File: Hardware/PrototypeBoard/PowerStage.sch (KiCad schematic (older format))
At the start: 20 parts, among them Q1 IRF8721PBF-1, Q2 IRF8721PBF-1, Q3 IRF8721PBF-1, Q4 IRF8721PBF-1, Q5 IRF8721PBF-1, Q6 IRF8721PBF-1

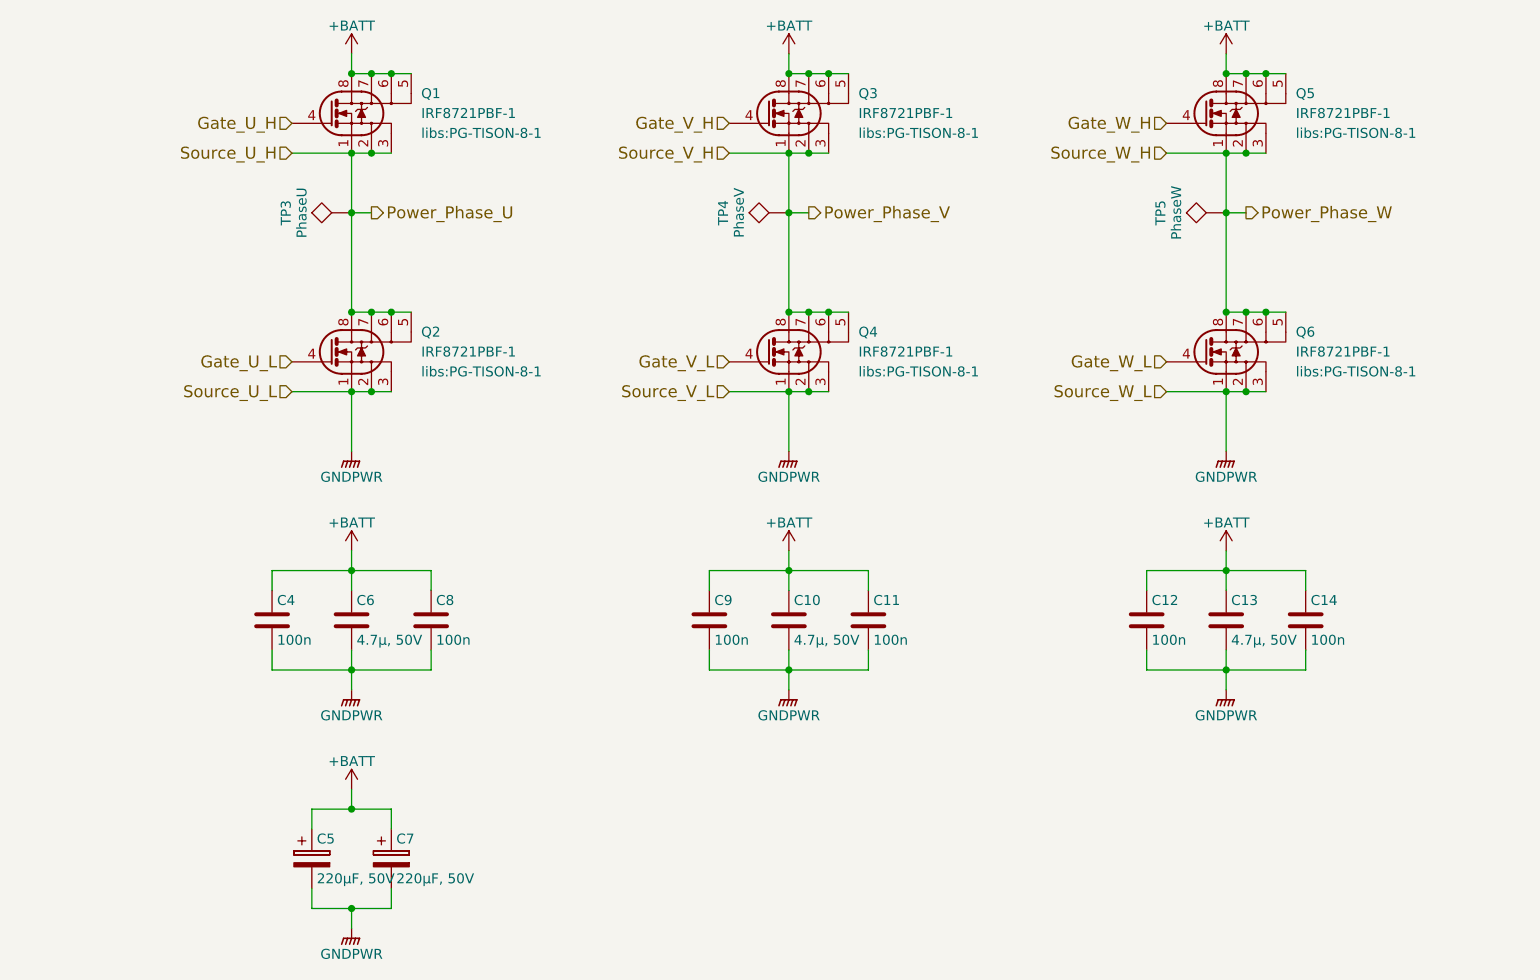
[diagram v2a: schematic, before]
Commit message: Added footprint for power MOSFETs
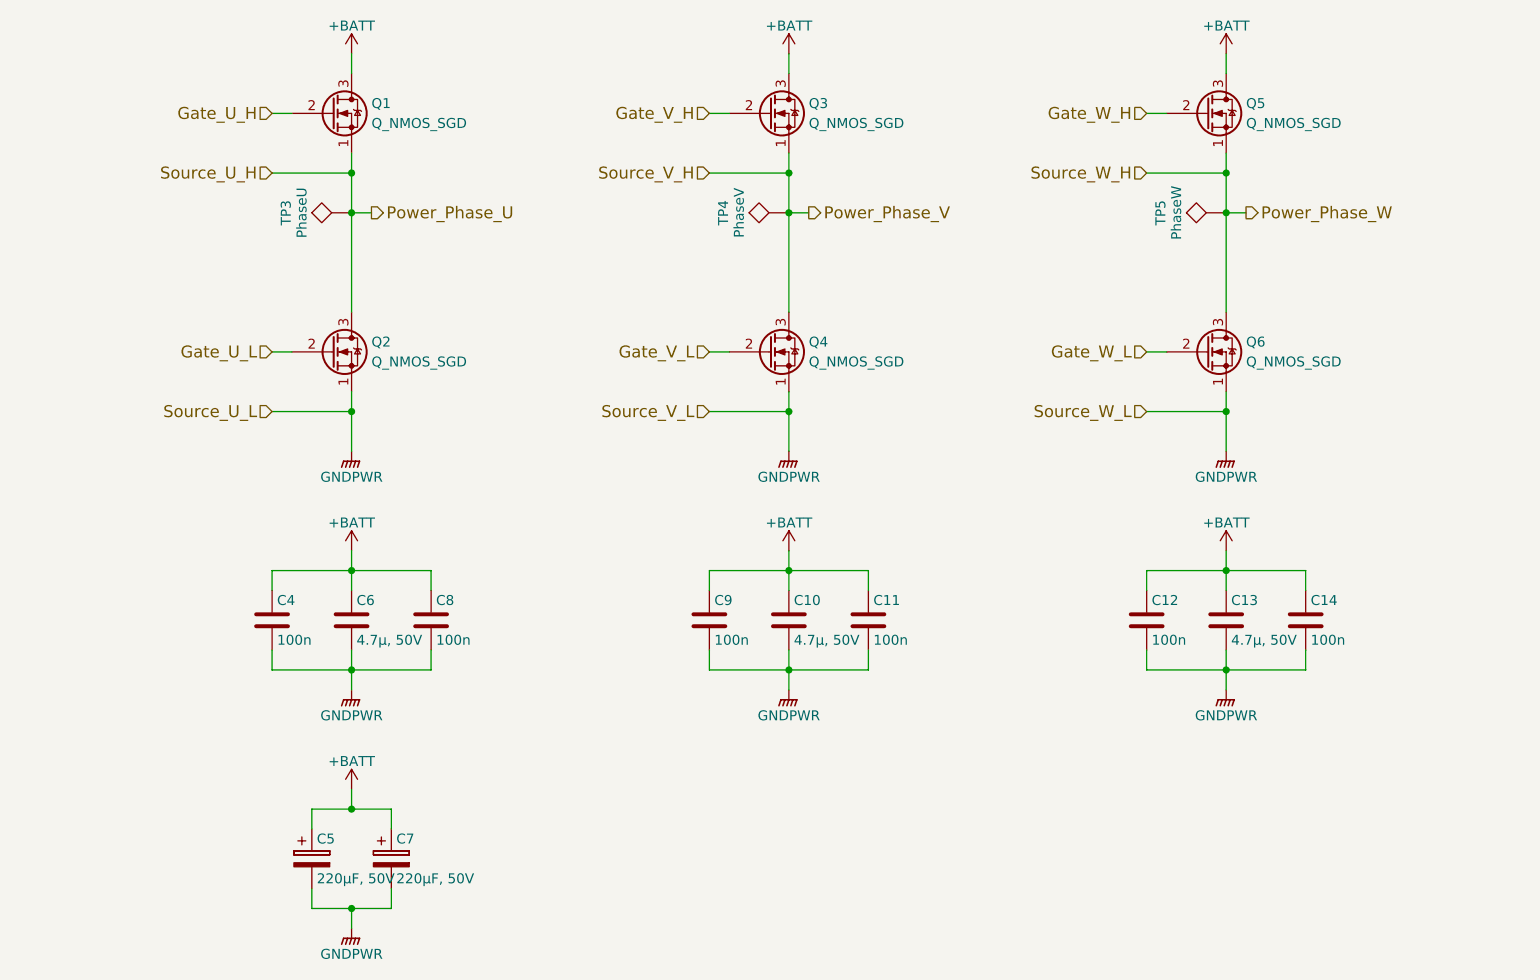
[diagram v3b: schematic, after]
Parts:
- removed Q1, Q2, Q3, Q4, Q5, Q6: IRF8721PBF-1, libs:PG-TISON-8-1, symbol IRF8721PBF-1
- added Q1, Q2, Q3, Q4, Q5, Q6: Q_NMOS_SGD, symbol Q_NMOS_SGD
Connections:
- net +BATT: now also Q1.3 (D), Q3.3 (D), Q5.3 (D)
- net GNDPWR: now also Q2.1 (S), Q4.1 (S), Q6.1 (S)
- net Gate_U_H: now also Q1.2 (G)
- net Gate_U_L: now also Q2.2 (G)
- net Gate_V_H: now also Q3.2 (G)
- net Gate_V_L: now also Q4.2 (G)
- net Gate_W_H: now also Q5.2 (G)
- net Gate_W_L: now also Q6.2 (G)
- net Power_Phase_U: now also Q1.1 (S), Q2.3 (D)
- net Power_Phase_V: now also Q3.1 (S), Q4.3 (D)
- net Power_Phase_W: now also Q5.1 (S), Q6.3 (D)
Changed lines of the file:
@@
 $EndDescr
 $Comp
-L IRF8721PBF-1 Q5
-U 1 1 56C10AD6
-P 7500 2400
-F 0 "Q5" H 7850 2500 50  0000 L CNN
-F 1 "IRF8721PBF-1" H 7850 2400 50  0000 L CNN
-F 2 "libs:PG-TISON-8-1" H 7850 2300 50  0000 L CNN
-F 3 "" H 7400 2400 50  0000 L CNN
-	1    7500 2400
-	1    0    0    -1
-$EndComp
-$Comp
-L IRF8721PBF-1 Q6
-U 1 1 56C10ADD
-P 7500 3600
-F 0 "Q6" H 7850 3700 50  0000 L CNN
-F 1 "IRF8721PBF-1" H 7850 3600 50  0000 L CNN
-F 2 "libs:PG-TISON-8-1" H 7850 3500 50  0000 L CNN
-F 3 "" H 7400 3600 50  0000 L CNN
-	1    7500 3600
-	1    0    0    -1
-$EndComp
-$Comp
-L IRF8721PBF-1 Q4
-U 1 1 56C10AE4
-P 5300 3600
-F 0 "Q4" H 5650 3700 50  0000 L CNN
-F 1 "IRF8721PBF-1" H 5650 3600 50  0000 L CNN
-F 2 "libs:PG-TISON-8-1" H 5650 3500 50  0000 L CNN
-F 3 "" H 5200 3600 50  0000 L CNN
-	1    5300 3600
-	1    0    0    -1
-$EndComp
-$Comp
-L IRF8721PBF-1 Q3
-U 1 1 56C10AEB
-P 5300 2400
-F 0 "Q3" H 5650 2500 50  0000 L CNN
-F 1 "IRF8721PBF-1" H 5650 2400 50  0000 L CNN
-F 2 "libs:PG-TISON-8-1" H 5650 2300 50  0000 L CNN
-F 3 "" H 5200 2400 50  0000 L CNN
-	1    5300 2400
-	1    0    0    -1
-$EndComp
-$Comp
-L IRF8721PBF-1 Q1
-U 1 1 56C10AF2
-P 3100 2400
-F 0 "Q1" H 3450 2500 50  0000 L CNN
-F 1 "IRF8721PBF-1" H 3450 2400 50  0000 L CNN
-F 2 "libs:PG-TISON-8-1" H 3450 2300 50  0000 L CNN
-F 3 "" H 3000 2400 50  0000 L CNN
-	1    3100 2400
-	1    0    0    -1
-$EndComp
-$Comp
-L IRF8721PBF-1 Q2
-U 1 1 56C10AF9
-P 3100 3600
-F 0 "Q2" H 3450 3700 50  0000 L CNN
-F 1 "IRF8721PBF-1" H 3450 3600 50  0000 L CNN
-F 2 "libs:PG-TISON-8-1" H 3450 3500 50  0000 L CNN
-F 3 "" H 3000 3600 50  0000 L CNN
-	1    3100 3600
-	1    0    0    -1
-$EndComp
-$Comp
-L GNDPWR #PWR012
+L GNDPWR #PWR13
 U 1 1 56C10B12
 P 3100 4100
-F 0 "#PWR012" H 3100 3900 50  0001 C CNN
+F 0 "#PWR13" H 3100 3900 50  0001 C CNN
 F 1 "GNDPWR" H 3100 3970 50  0000 C CNN
 F 2 "" H 3100 4050 50  0000 C CNN
@@
 $EndComp
 $Comp
-L GNDPWR #PWR013
+L GNDPWR #PWR19
 U 1 1 56C10B18
 P 5300 4100
-F 0 "#PWR013" H 5300 3900 50  0001 C CNN
+F 0 "#PWR19" H 5300 3900 50  0001 C CNN
 F 1 "GNDPWR" H 5300 3970 50  0000 C CNN
 F 2 "" H 5300 4050 50  0000 C CNN
@@
 $EndComp
 $Comp
-L GNDPWR #PWR014
+L GNDPWR #PWR23
 U 1 1 56C10B1E
 P 7500 4100
-F 0 "#PWR014" H 7500 3900 50  0001 C CNN
+F 0 "#PWR23" H 7500 3900 50  0001 C CNN
 F 1 "GNDPWR" H 7500 3970 50  0000 C CNN
 F 2 "" H 7500 4050 50  0000 C CNN
@@
 Text HLabel 5400 2900 2    60   Output ~ 0
 Power_Phase_V
-Text HLabel 2800 2450 0    60   Input ~ 0
+Text HLabel 2700 2400 0    60   Input ~ 0
 Gate_U_H
-Text HLabel 2800 3650 0    60   Input ~ 0
+Text HLabel 2700 3600 0    60   Input ~ 0
 Gate_U_L
-Text HLabel 5000 2450 0    60   Input ~ 0
+Text HLabel 4900 2400 0    60   Input ~ 0
 Gate_V_H
-Text HLabel 5000 3650 0    60   Input ~ 0
+Text HLabel 4900 3600 0    60   Input ~ 0
 Gate_V_L
-Text HLabel 7200 2450 0    60   Input ~ 0
+Text HLabel 7100 2400 0    60   Input ~ 0
 Gate_W_H
-Text HLabel 7200 3650 0    60   Input ~ 0
+Text HLabel 7100 3600 0    60   Input ~ 0
 Gate_W_L
-Text HLabel 2800 3800 0    60   Input ~ 0
+Text HLabel 2700 3900 0    60   Input ~ 0
 Source_U_L
-Text HLabel 2800 2600 0    60   Input ~ 0
+Text HLabel 2700 2700 0    60   Input ~ 0
 Source_U_H
-Text HLabel 5000 2600 0    60   Input ~ 0
+Text HLabel 4900 2700 0    60   Input ~ 0
 Source_V_H
-Text HLabel 5000 3800 0    60   Input ~ 0
+Text HLabel 4900 3900 0    60   Input ~ 0
 Source_V_L
-Text HLabel 7200 2600 0    60   Input ~ 0
+Text HLabel 7100 2700 0    60   Input ~ 0
 Source_W_H
-Text HLabel 7200 3800 0    60   Input ~ 0
+Text HLabel 7100 3900 0    60   Input ~ 0
 Source_W_L
 $Comp
-L +BATT #PWR015
+L +BATT #PWR18
 U 1 1 56C3D45F
 P 5300 2100
-F 0 "#PWR015" H 5300 1950 50  0001 C CNN
+F 0 "#PWR18" H 5300 1950 50  0001 C CNN
 F 1 "+BATT" H 5300 2240 50  0000 C CNN
 F 2 "" H 5300 2100 50  0000 C CNN
@@
 $EndComp
 $Comp
-L +BATT #PWR016
+L +BATT #PWR12
 U 1 1 56C3D47F
 P 3100 2100
-F 0 "#PWR016" H 3100 1950 50  0001 C CNN
+F 0 "#PWR12" H 3100 1950 50  0001 C CNN
 F 1 "+BATT" H 3100 2240 50  0000 C CNN
 F 2 "" H 3100 2100 50  0000 C CNN
@@
 $EndComp
 $Comp
-L +BATT #PWR017
+L +BATT #PWR22
 U 1 1 56C3D49F
 P 7500 2100
-F 0 "#PWR017" H 7500 1950 50  0001 C CNN
+F 0 "#PWR22" H 7500 1950 50  0001 C CNN
 F 1 "+BATT" H 7500 2240 50  0000 C CNN
 F 2 "" H 7500 2100 50  0000 C CNN
@@
 $EndComp
 $Comp
-L GNDPWR #PWR018
+L GNDPWR #PWR15
 U 1 1 5B00BA7D
 P 3100 5300
-F 0 "#PWR018" H 3100 5100 50  0001 C CNN
+F 0 "#PWR15" H 3100 5100 50  0001 C CNN
 F 1 "GNDPWR" H 3100 5170 50  0000 C CNN
 F 2 "" H 3100 5250 50  0000 C CNN
@@
 $EndComp
 $Comp
-L GNDPWR #PWR019
+L GNDPWR #PWR21
 U 1 1 5B00BB28
 P 5300 5300
-F 0 "#PWR019" H 5300 5100 50  0001 C CNN
+F 0 "#PWR21" H 5300 5100 50  0001 C CNN
 F 1 "GNDPWR" H 5300 5170 50  0000 C CNN
 F 2 "" H 5300 5250 50  0000 C CNN
@@
 $EndComp
 $Comp
-L GNDPWR #PWR020
+L GNDPWR #PWR25
 U 1 1 5B00BB6F
 P 7500 5300
-F 0 "#PWR020" H 7500 5100 50  0001 C CNN
+F 0 "#PWR25" H 7500 5100 50  0001 C CNN
 F 1 "GNDPWR" H 7500 5170 50  0000 C CNN
 F 2 "" H 7500 5250 50  0000 C CNN
@@
 $EndComp
 $Comp
-L GNDPWR #PWR021
+L GNDPWR #PWR17
 U 1 1 5B00BBB6
 P 3100 6500
-F 0 "#PWR021" H 3100 6300 50  0001 C CNN
+F 0 "#PWR17" H 3100 6300 50  0001 C CNN
 F 1 "GNDPWR" H 3100 6370 50  0000 C CNN
 F 2 "" H 3100 6450 50  0000 C CNN
@@
 $EndComp
 Wire Wire Line
-	3100 2200 3400 2200
-Connection ~ 3200 2200
-Connection ~ 3300 2200
-Wire Wire Line
 	3100 2600 3100 3400
 Wire Wire Line
-	2800 2600 3300 2600
-Connection ~ 3200 2600
-Wire Wire Line
-	3100 3400 3400 3400
-Connection ~ 3200 3400
-Connection ~ 3300 3400
-Wire Wire Line
 	5300 2600 5300 3400
 Wire Wire Line
-	5300 3400 5600 3400
-Connection ~ 5400 3400
-Connection ~ 5500 3400
-Wire Wire Line
-	5000 2600 5500 2600
-Connection ~ 5400 2600
-Wire Wire Line
-	2800 3800 3300 3800
-Connection ~ 3200 3800
-Wire Wire Line
-	5000 3800 5500 3800
-Connection ~ 5400 3800
-Wire Wire Line
-	7500 2200 7800 2200
-Connection ~ 7600 2200
-Connection ~ 7700 2200
-Wire Wire Line
 	7500 2600 7500 3400
-Wire Wire Line
-	7500 3400 7800 3400
-Connection ~ 7600 3400
-Connection ~ 7700 3400
-Wire Wire Line
-	7200 2600 7700 2600
-Connection ~ 7600 2600
-Wire Wire Line
-	7200 3800 7700 3800
-Connection ~ 7600 3800
-Wire Wire Line
-	5300 2200 5600 2200
-Connection ~ 5400 2200
-Connection ~ 5500 2200
-Connection ~ 5300 2200
-Connection ~ 3100 2200
-Connection ~ 3100 3400
-Connection ~ 5300 3400
-Connection ~ 5300 3800
-Connection ~ 3100 3800
-Connection ~ 7500 3800
-Connection ~ 7500 3400
-Connection ~ 7500 2200
-Connection ~ 5300 2600
-Connection ~ 3100 2600
-Connection ~ 7500 2600
 Wire Wire Line
 	3100 2900 3200 2900
@@
 Connection ~ 3100 6400
 $Comp
-L +BATT #PWR022
+L +BATT #PWR14
 U 1 1 5B00C18C
 P 3100 4600
-F 0 "#PWR022" H 3100 4450 50  0001 C CNN
+F 0 "#PWR14" H 3100 4450 50  0001 C CNN
 F 1 "+BATT" H 3100 4740 50  0000 C CNN
 F 2 "" H 3100 4600 50  0000 C CNN
@@
 $EndComp
 $Comp
-L +BATT #PWR023
+L +BATT #PWR20
 U 1 1 5B00C1D3
 P 5300 4600
-F 0 "#PWR023" H 5300 4450 50  0001 C CNN
+F 0 "#PWR20" H 5300 4450 50  0001 C CNN
 F 1 "+BATT" H 5300 4740 50  0000 C CNN
 F 2 "" H 5300 4600 50  0000 C CNN
@@
 $EndComp
 $Comp
-L +BATT #PWR024
+L +BATT #PWR24
 U 1 1 5B00C21A
 P 7500 4600
-F 0 "#PWR024" H 7500 4450 50  0001 C CNN
+F 0 "#PWR24" H 7500 4450 50  0001 C CNN
 F 1 "+BATT" H 7500 4740 50  0000 C CNN
 F 2 "" H 7500 4600 50  0000 C CNN
@@
 $EndComp
 $Comp
-L +BATT #PWR025
+L +BATT #PWR16
 U 1 1 5B00C9A4
 P 3100 5800
-F 0 "#PWR025" H 3100 5650 50  0001 C CNN
+F 0 "#PWR16" H 3100 5650 50  0001 C CNN
 F 1 "+BATT" H 3100 5940 50  0000 C CNN
 F 2 "" H 3100 5800 50  0000 C CNN
@@
 	3100 5800 3100 5900
 Connection ~ 3100 5900
+$Comp
+L Q_NMOS_SGD Q1
+U 1 1 5B00718F
+P 3000 2400
+F 0 "Q1" H 3200 2450 50  0000 L CNN
+F 1 "Q_NMOS_SGD" H 3200 2350 50  0000 L CNN
+F 2 "" H 3200 2500 50  0001 C CNN
+F 3 "" H 3000 2400 50  0001 C CNN
+	1    3000 2400
+	1    0    0    -1
+$EndComp
+$Comp
+L Q_NMOS_SGD Q2
+U 1 1 5B00724E
+P 3000 3600
+F 0 "Q2" H 3200 3650 50  0000 L CNN
+F 1 "Q_NMOS_SGD" H 3200 3550 50  0000 L CNN
+F 2 "" H 3200 3700 50  0001 C CNN
+F 3 "" H 3000 3600 50  0001 C CNN
+	1    3000 3600
+	1    0    0    -1
+$EndComp
+$Comp
+L Q_NMOS_SGD Q4
+U 1 1 5B0072F2
+P 5200 3600
+F 0 "Q4" H 5400 3650 50  0000 L CNN
+F 1 "Q_NMOS_SGD" H 5400 3550 50  0000 L CNN
+F 2 "" H 5400 3700 50  0001 C CNN
+F 3 "" H 5200 3600 50  0001 C CNN
+	1    5200 3600
+	1    0    0    -1
+$EndComp
+$Comp
+L Q_NMOS_SGD Q3
+U 1 1 5B007385
+P 5200 2400
+F 0 "Q3" H 5400 2450 50  0000 L CNN
+F 1 "Q_NMOS_SGD" H 5400 2350 50  0000 L CNN
+F 2 "" H 5400 2500 50  0001 C CNN
+F 3 "" H 5200 2400 50  0001 C CNN
+	1    5200 2400
+	1    0    0    -1
+$EndComp
+$Comp
+L Q_NMOS_SGD Q5
+U 1 1 5B0073FB
+P 7400 2400
+F 0 "Q5" H 7600 2450 50  0000 L CNN
+F 1 "Q_NMOS_SGD" H 7600 2350 50  0000 L CNN
+F 2 "" H 7600 2500 50  0001 C CNN
+F 3 "" H 7400 2400 50  0001 C CNN
+	1    7400 2400
+	1    0    0    -1
+$EndComp
+$Comp
+L Q_NMOS_SGD Q6
+U 1 1 5B00749A
+P 7400 3600
+F 0 "Q6" H 7600 3650 50  0000 L CNN
+F 1 "Q_NMOS_SGD" H 7600 3550 50  0000 L CNN
+F 2 "" H 7600 3700 50  0001 C CNN
+F 3 "" H 7400 3600 50  0001 C CNN
+	1    7400 3600
+	1    0    0    -1
+$EndComp
+Wire Wire Line
+	2700 2400 2800 2400
+Wire Wire Line
+	2700 2700 3100 2700
+Connection ~ 3100 2700
+Wire Wire Line
+	2700 3600 2800 3600
+Wire Wire Line
+	2700 3900 3100 3900
+Connection ~ 3100 3900
+Wire Wire Line
+	4900 2400 5000 2400
+Wire Wire Line
+	4900 2700 5300 2700
+Connection ~ 5300 2700
+Wire Wire Line
+	4900 3600 5000 3600
+Wire Wire Line
+	4900 3900 5300 3900
+Connection ~ 5300 3900
+Wire Wire Line
+	7100 2400 7200 2400
+Wire Wire Line
+	7100 2700 7500 2700
+Connection ~ 7500 2700
+Wire Wire Line
+	7100 3600 7200 3600
+Wire Wire Line
+	7100 3900 7500 3900
+Connection ~ 7500 3900
 $EndSCHEMATC

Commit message: Corrected paste layer of footprints, deleted unnecessary files
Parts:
- Q1, Q2, Q3, Q4, Q5, Q6: footprint (none) -> libs:TDSON-8_FL
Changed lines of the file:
@@
 $EndDescr
 $Comp
-L GNDPWR #PWR13
+L GNDPWR #PWR012
 U 1 1 56C10B12
 P 3100 4100
-F 0 "#PWR13" H 3100 3900 50  0001 C CNN
+F 0 "#PWR012" H 3100 3900 50  0001 C CNN
 F 1 "GNDPWR" H 3100 3970 50  0000 C CNN
 F 2 "" H 3100 4050 50  0000 C CNN
@@
 $EndComp
 $Comp
-L GNDPWR #PWR19
+L GNDPWR #PWR013
 U 1 1 56C10B18
 P 5300 4100
-F 0 "#PWR19" H 5300 3900 50  0001 C CNN
+F 0 "#PWR013" H 5300 3900 50  0001 C CNN
 F 1 "GNDPWR" H 5300 3970 50  0000 C CNN
 F 2 "" H 5300 4050 50  0000 C CNN
@@
 $EndComp
 $Comp
-L GNDPWR #PWR23
+L GNDPWR #PWR014
 U 1 1 56C10B1E
 P 7500 4100
-F 0 "#PWR23" H 7500 3900 50  0001 C CNN
+F 0 "#PWR014" H 7500 3900 50  0001 C CNN
 F 1 "GNDPWR" H 7500 3970 50  0000 C CNN
 F 2 "" H 7500 4050 50  0000 C CNN
@@
 Source_W_L
 $Comp
-L +BATT #PWR18
+L +BATT #PWR015
 U 1 1 56C3D45F
 P 5300 2100
-F 0 "#PWR18" H 5300 1950 50  0001 C CNN
+F 0 "#PWR015" H 5300 1950 50  0001 C CNN
 F 1 "+BATT" H 5300 2240 50  0000 C CNN
 F 2 "" H 5300 2100 50  0000 C CNN
@@
 $EndComp
 $Comp
-L +BATT #PWR12
+L +BATT #PWR016
 U 1 1 56C3D47F
 P 3100 2100
-F 0 "#PWR12" H 3100 1950 50  0001 C CNN
+F 0 "#PWR016" H 3100 1950 50  0001 C CNN
 F 1 "+BATT" H 3100 2240 50  0000 C CNN
 F 2 "" H 3100 2100 50  0000 C CNN
@@
 $EndComp
 $Comp
-L +BATT #PWR22
+L +BATT #PWR017
 U 1 1 56C3D49F
 P 7500 2100
-F 0 "#PWR22" H 7500 1950 50  0001 C CNN
+F 0 "#PWR017" H 7500 1950 50  0001 C CNN
 F 1 "+BATT" H 7500 2240 50  0000 C CNN
 F 2 "" H 7500 2100 50  0000 C CNN
@@
 $EndComp
 $Comp
-L GNDPWR #PWR15
+L GNDPWR #PWR018
 U 1 1 5B00BA7D
 P 3100 5300
-F 0 "#PWR15" H 3100 5100 50  0001 C CNN
+F 0 "#PWR018" H 3100 5100 50  0001 C CNN
 F 1 "GNDPWR" H 3100 5170 50  0000 C CNN
 F 2 "" H 3100 5250 50  0000 C CNN
@@
 $EndComp
 $Comp
-L GNDPWR #PWR21
+L GNDPWR #PWR019
 U 1 1 5B00BB28
 P 5300 5300
-F 0 "#PWR21" H 5300 5100 50  0001 C CNN
+F 0 "#PWR019" H 5300 5100 50  0001 C CNN
 F 1 "GNDPWR" H 5300 5170 50  0000 C CNN
 F 2 "" H 5300 5250 50  0000 C CNN
@@
 $EndComp
 $Comp
-L GNDPWR #PWR25
+L GNDPWR #PWR020
 U 1 1 5B00BB6F
 P 7500 5300
-F 0 "#PWR25" H 7500 5100 50  0001 C CNN
+F 0 "#PWR020" H 7500 5100 50  0001 C CNN
 F 1 "GNDPWR" H 7500 5170 50  0000 C CNN
 F 2 "" H 7500 5250 50  0000 C CNN
@@
 $EndComp
 $Comp
-L GNDPWR #PWR17
+L GNDPWR #PWR021
 U 1 1 5B00BBB6
 P 3100 6500
-F 0 "#PWR17" H 3100 6300 50  0001 C CNN
+F 0 "#PWR021" H 3100 6300 50  0001 C CNN
 F 1 "GNDPWR" H 3100 6370 50  0000 C CNN
 F 2 "" H 3100 6450 50  0000 C CNN
@@
 Connection ~ 3100 6400
 $Comp
-L +BATT #PWR14
+L +BATT #PWR022
 U 1 1 5B00C18C
 P 3100 4600
-F 0 "#PWR14" H 3100 4450 50  0001 C CNN
+F 0 "#PWR022" H 3100 4450 50  0001 C CNN
 F 1 "+BATT" H 3100 4740 50  0000 C CNN
 F 2 "" H 3100 4600 50  0000 C CNN
@@
 $EndComp
 $Comp
-L +BATT #PWR20
+L +BATT #PWR023
 U 1 1 5B00C1D3
 P 5300 4600
-F 0 "#PWR20" H 5300 4450 50  0001 C CNN
+F 0 "#PWR023" H 5300 4450 50  0001 C CNN
 F 1 "+BATT" H 5300 4740 50  0000 C CNN
 F 2 "" H 5300 4600 50  0000 C CNN
@@
 $EndComp
 $Comp
-L +BATT #PWR24
+L +BATT #PWR024
 U 1 1 5B00C21A
 P 7500 4600
-F 0 "#PWR24" H 7500 4450 50  0001 C CNN
+F 0 "#PWR024" H 7500 4450 50  0001 C CNN
 F 1 "+BATT" H 7500 4740 50  0000 C CNN
 F 2 "" H 7500 4600 50  0000 C CNN
@@
 $EndComp
 $Comp
-L +BATT #PWR16
+L +BATT #PWR025
 U 1 1 5B00C9A4
 P 3100 5800
-F 0 "#PWR16" H 3100 5650 50  0001 C CNN
+F 0 "#PWR025" H 3100 5650 50  0001 C CNN
 F 1 "+BATT" H 3100 5940 50  0000 C CNN
 F 2 "" H 3100 5800 50  0000 C CNN
@@
 F 0 "Q1" H 3200 2450 50  0000 L CNN
 F 1 "Q_NMOS_SGD" H 3200 2350 50  0000 L CNN
-F 2 "" H 3200 2500 50  0001 C CNN
+F 2 "libs:TDSON-8_FL" H 3200 2500 50  0001 C CNN
 F 3 "" H 3000 2400 50  0001 C CNN
 	1    3000 2400
@@
 F 0 "Q2" H 3200 3650 50  0000 L CNN
 F 1 "Q_NMOS_SGD" H 3200 3550 50  0000 L CNN
-F 2 "" H 3200 3700 50  0001 C CNN
+F 2 "libs:TDSON-8_FL" H 3200 3700 50  0001 C CNN
 F 3 "" H 3000 3600 50  0001 C CNN
 	1    3000 3600
@@
 F 0 "Q4" H 5400 3650 50  0000 L CNN
 F 1 "Q_NMOS_SGD" H 5400 3550 50  0000 L CNN
-F 2 "" H 5400 3700 50  0001 C CNN
+F 2 "libs:TDSON-8_FL" H 5400 3700 50  0001 C CNN
 F 3 "" H 5200 3600 50  0001 C CNN
 	1    5200 3600
@@
 F 0 "Q3" H 5400 2450 50  0000 L CNN
 F 1 "Q_NMOS_SGD" H 5400 2350 50  0000 L CNN
-F 2 "" H 5400 2500 50  0001 C CNN
+F 2 "libs:TDSON-8_FL" H 5400 2500 50  0001 C CNN
 F 3 "" H 5200 2400 50  0001 C CNN
 	1    5200 2400
@@
 F 0 "Q5" H 7600 2450 50  0000 L CNN
 F 1 "Q_NMOS_SGD" H 7600 2350 50  0000 L CNN
-F 2 "" H 7600 2500 50  0001 C CNN
+F 2 "libs:TDSON-8_FL" H 7600 2500 50  0001 C CNN
 F 3 "" H 7400 2400 50  0001 C CNN
 	1    7400 2400
@@
 F 0 "Q6" H 7600 3650 50  0000 L CNN
 F 1 "Q_NMOS_SGD" H 7600 3550 50  0000 L CNN
-F 2 "" H 7600 3700 50  0001 C CNN
+F 2 "libs:TDSON-8_FL" H 7600 3700 50  0001 C CNN
 F 3 "" H 7400 3600 50  0001 C CNN
 	1    7400 3600
